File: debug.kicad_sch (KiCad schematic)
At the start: 4 parts, among them J3 FTSH-105-01-L-DV-007

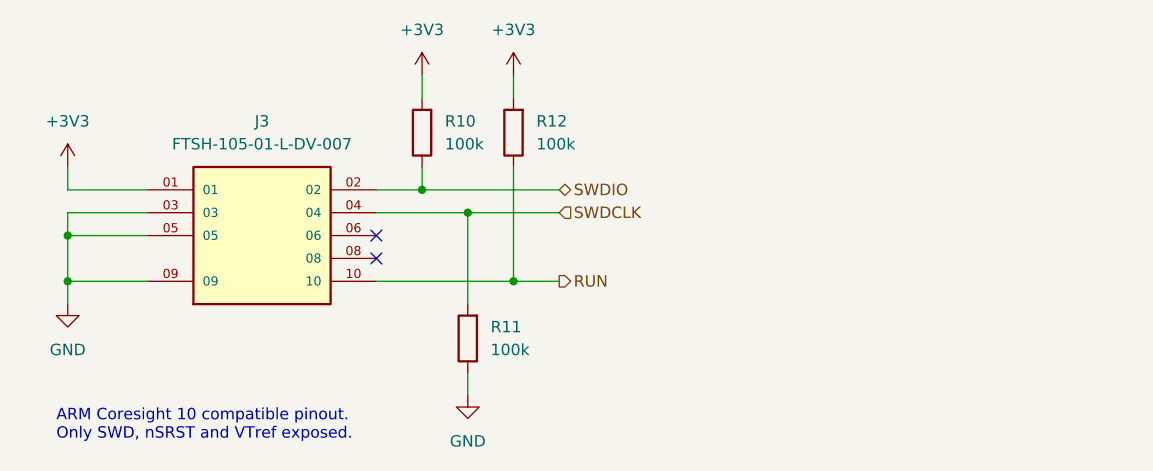
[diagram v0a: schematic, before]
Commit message: Block diagram
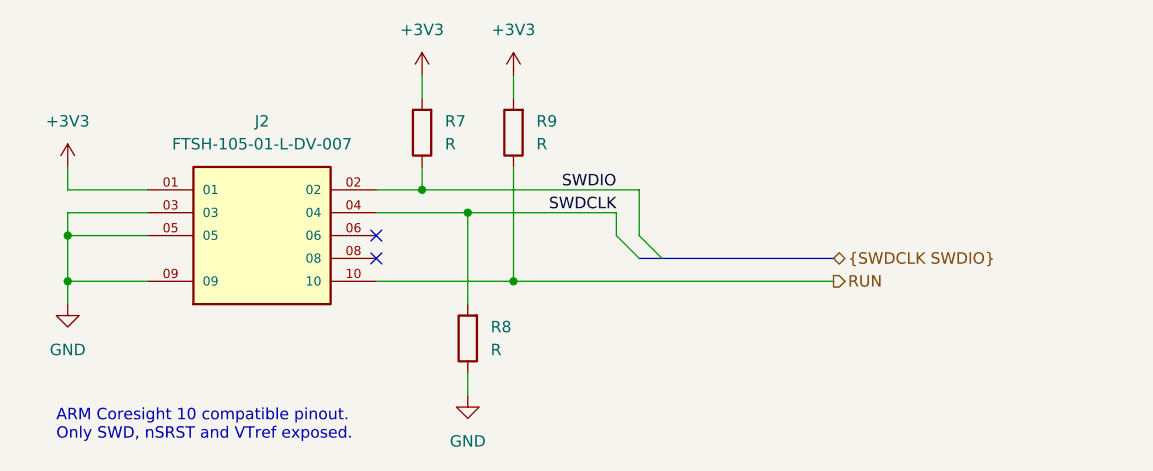
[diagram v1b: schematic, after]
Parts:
- R7: renamed from R10; value 100k -> R; footprint Resistor_SMD:R_1206_3216Metric -> Resistor_SMD:R_0402_1005Metric
- R8: renamed from R11; value 100k -> R; footprint Resistor_SMD:R_1206_3216Metric -> Resistor_SMD:R_0402_1005Metric
- R9: renamed from R12; value 100k -> R; footprint Resistor_SMD:R_1206_3216Metric -> Resistor_SMD:R_0402_1005Metric
- renumbered J3 to J2
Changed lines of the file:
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@@
 		(at 139.7 95.25)
 	)
+	(bus_entry
+		(at 166.37 95.25)
+		(size 2.54 2.54)
+		(stroke
+			(width 0)
+			(type default)
+		)
+	)
+	(bus_entry
+		(at 168.91 95.25)
+		(size 2.54 2.54)
+		(stroke
+			(width 0)
+			(type default)
+		)
+	)
 	(wire
 		(pts
@@
 	(wire
 		(pts
-			(xy 160.02 90.17) (xy 144.78 90.17)
+			(xy 144.78 90.17) (xy 168.91 90.17)
 		)
 		(stroke
@@
 	(wire
 		(pts
+			(xy 166.37 92.71) (xy 166.37 95.25)
+		)
+		(stroke
+			(width 0)
+			(type default)
+		)
+	)
+	(wire
+		(pts
 			(xy 139.7 100.33) (xy 154.94 100.33)
 		)
@@
 	(wire
 		(pts
-			(xy 149.86 92.71) (xy 160.02 92.71)
-		)
-		(stroke
-			(width 0)
-			(type default)
-		)
-	)
-	(wire
-		(pts
-			(xy 160.02 100.33) (xy 154.94 100.33)
+			(xy 149.86 92.71) (xy 166.37 92.71)
+		)
+		(stroke
+			(width 0)
+			(type default)
+		)
+	)
+	(wire
+		(pts
+			(xy 168.91 90.17) (xy 168.91 95.25)
+		)
+		(stroke
+			(width 0)
+			(type default)
+		)
+	)
+	(wire
+		(pts
+			(xy 190.5 100.33) (xy 154.94 100.33)
+		)
+		(stroke
+			(width 0)
+			(type default)
+		)
+	)
+	(bus
+		(pts
+			(xy 171.45 97.79) (xy 190.5 97.79)
 		)
 		(stroke
@@
 		(pts
 			(xy 149.86 110.49) (xy 149.86 113.03)
+		)
+		(stroke
+			(width 0)
+			(type default)
+		)
+	)
+	(bus
+		(pts
+			(xy 168.91 97.79) (xy 171.45 97.79)
 		)
 		(stroke
@@
 		)
 	)
-	(hierarchical_label "SWDCLK"
-		(shape input)
-		(at 160.02 92.71 0)
+	(label "SWDIO"
+		(at 166.37 90.17 180)
 		(fields_autoplaced yes)
 		(effects
@@
 				(size 1.27 1.27)
 			)
-			(justify left)
-		)
-	)
-	(hierarchical_label "SWDIO"
-		(shape bidirectional)
-		(at 160.02 90.17 0)
+			(justify right bottom)
+		)
+	)
+	(label "SWDCLK"
+		(at 166.37 92.71 180)
 		(fields_autoplaced yes)
 		(effects
@@
 				(size 1.27 1.27)
 			)
+			(justify right bottom)
+		)
+	)
+	(hierarchical_label "{SWDCLK SWDIO}"
+		(shape bidirectional)
+		(at 190.5 97.79 0)
+		(fields_autoplaced yes)
+		(effects
+			(font
+				(size 1.27 1.27)
+			)
 			(justify left)
 		)
@@
 	(hierarchical_label "RUN"
 		(shape output)
-		(at 160.02 100.33 0)
+		(at 190.5 100.33 0)
 		(fields_autoplaced yes)
 		(effects
@@
 		(dnp no)
 		(fields_autoplaced yes)
-		(property "Reference" "R11"
+		(property "Reference" "R8"
 			(at 152.4 105.41 0)
 			(effects
@@
 			)
 		)
-		(property "Value" "100k"
+		(property "Value" "R"
 			(at 152.4 107.95 0)
 			(effects
@@
 			)
 		)
-		(property "Footprint" "Resistor_SMD:R_1206_3216Metric"
+		(property "Footprint" "Resistor_SMD:R_0402_1005Metric"
 			(at 151.638 106.68 90)
 			(effects
@@
 			)
 		)
-		(property "Description" ""
+		(property "Description" "Resistor"
 			(at 149.86 106.68 0)
 			(effects
@@
 			(project "cubesat_rp2040"
 				(path "/5511013b-c214-40ba-8960-f470f52474f8/5047da3d-75a3-46e1-87b7-3e807ce5a802"
-					(reference "R11")
+					(reference "R8")
 					(unit 1)
 				)
@@
 		(dnp no)
 		(fields_autoplaced yes)
-		(property "Reference" "J3"
+		(property "Reference" "J2"
 			(at 127 82.55 0)
 			(effects
@@
 			(project "cubesat_rp2040"
 				(path "/5511013b-c214-40ba-8960-f470f52474f8/5047da3d-75a3-46e1-87b7-3e807ce5a802"
-					(reference "J3")
+					(reference "J2")
 					(unit 1)
 				)
@@
 		(dnp no)
 		(fields_autoplaced yes)
-		(property "Reference" "#PWR029"
+		(property "Reference" "#PWR019"
 			(at 154.94 81.28 0)
 			(effects
@@
 			)
 		)
-		(property "Description" ""
+		(property "Description" "Power symbol creates a global label with name \"+3V3\""
 			(at 154.94 77.47 0)
 			(effects
@@
 			(project "cubesat_rp2040"
 				(path "/5511013b-c214-40ba-8960-f470f52474f8/5047da3d-75a3-46e1-87b7-3e807ce5a802"
-					(reference "#PWR029")
+					(reference "#PWR019")
 					(unit 1)
 				)
@@
 		(dnp no)
 		(fields_autoplaced yes)
-		(property "Reference" "#PWR026"
+		(property "Reference" "#PWR016"
 			(at 105.41 109.22 0)
 			(effects
@@
 			)
 		)
-		(property "Description" ""
+		(property "Description" "Power symbol creates a global label with name \"GND\" , ground"
 			(at 105.41 102.87 0)
 			(effects
@@
 			(project "cubesat_rp2040"
 				(path "/5511013b-c214-40ba-8960-f470f52474f8/5047da3d-75a3-46e1-87b7-3e807ce5a802"
-					(reference "#PWR026")
+					(reference "#PWR016")
 					(unit 1)
 				)
@@
 		(dnp no)
 		(fields_autoplaced yes)
-		(property "Reference" "#PWR028"
+		(property "Reference" "#PWR018"
 			(at 149.86 119.38 0)
 			(effects
@@
 			)
 		)
-		(property "Description" ""
+		(property "Description" "Power symbol creates a global label with name \"GND\" , ground"
 			(at 149.86 113.03 0)
 			(effects
@@
 			(project "cubesat_rp2040"
 				(path "/5511013b-c214-40ba-8960-f470f52474f8/5047da3d-75a3-46e1-87b7-3e807ce5a802"
-					(reference "#PWR028")
+					(reference "#PWR018")
 					(unit 1)
 				)
@@
 		(dnp no)
 		(fields_autoplaced yes)
-		(property "Reference" "R10"
+		(property "Reference" "R7"
 			(at 147.32 82.55 0)
 			(effects
@@
 			)
 		)
-		(property "Value" "100k"
+		(property "Value" "R"
 			(at 147.32 85.09 0)
 			(effects
@@
 			)
 		)
-		(property "Footprint" "Resistor_SMD:R_1206_3216Metric"
+		(property "Footprint" "Resistor_SMD:R_0402_1005Metric"
 			(at 146.558 83.82 90)
 			(effects
@@
 			)
 		)
-		(property "Description" ""
+		(property "Description" "Resistor"
 			(at 144.78 83.82 0)
 			(effects
@@
 			(project "cubesat_rp2040"
 				(path "/5511013b-c214-40ba-8960-f470f52474f8/5047da3d-75a3-46e1-87b7-3e807ce5a802"
-					(reference "R10")
+					(reference "R7")
 					(unit 1)
 				)
@@
 		(dnp no)
 		(fields_autoplaced yes)
-		(property "Reference" "#PWR025"
+		(property "Reference" "#PWR015"
 			(at 105.41 91.44 0)
 			(effects
@@
 			)
 		)
-		(property "Description" ""
+		(property "Description" "Power symbol creates a global label with name \"+3V3\""
 			(at 105.41 87.63 0)
 			(effects
@@
 			(project "cubesat_rp2040"
 				(path "/5511013b-c214-40ba-8960-f470f52474f8/5047da3d-75a3-46e1-87b7-3e807ce5a802"
-					(reference "#PWR025")
+					(reference "#PWR015")
 					(unit 1)
 				)
@@
 		(dnp no)
 		(fields_autoplaced yes)
-		(property "Reference" "#PWR027"
+		(property "Reference" "#PWR017"
 			(at 144.78 81.28 0)
 			(effects
@@
 			)
 		)
-		(property "Description" ""
+		(property "Description" "Power symbol creates a global label with name \"+3V3\""
 			(at 144.78 77.47 0)
 			(effects
@@
 			(project "cubesat_rp2040"
 				(path "/5511013b-c214-40ba-8960-f470f52474f8/5047da3d-75a3-46e1-87b7-3e807ce5a802"
-					(reference "#PWR027")
+					(reference "#PWR017")
 					(unit 1)
 				)
@@
 		(dnp no)
 		(fields_autoplaced yes)
-		(property "Reference" "R12"
+		(property "Reference" "R9"
 			(at 157.48 82.55 0)
 			(effects
@@
 			)
 		)
-		(property "Value" "100k"
+		(property "Value" "R"
 			(at 157.48 85.09 0)
 			(effects
@@
 			)
 		)
-		(property "Footprint" "Resistor_SMD:R_1206_3216Metric"
+		(property "Footprint" "Resistor_SMD:R_0402_1005Metric"
 			(at 156.718 83.82 90)
 			(effects
@@
 			)
 		)
-		(property "Description" ""
+		(property "Description" "Resistor"
 			(at 154.94 83.82 0)
 			(effects
@@
 			(project "cubesat_rp2040"
 				(path "/5511013b-c214-40ba-8960-f470f52474f8/5047da3d-75a3-46e1-87b7-3e807ce5a802"
-					(reference "R12")
+					(reference "R9")
 					(unit 1)
 				)

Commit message: Big update, bad commit messsage :)
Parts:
- J401: renamed from J2; symbol cubesat_rp2040:FTSH-105-01-L-DV-007 -> cubesat_rp2040:CoreSight_10_Conn
- R401: renamed from R7; footprint Resistor_SMD:R_0402_1005Metric -> cubesat_rp2040:R_0402_1005Metric
- R402: renamed from R8; footprint Resistor_SMD:R_0402_1005Metric -> cubesat_rp2040:R_0402_1005Metric
- R403: renamed from R9; footprint Resistor_SMD:R_0402_1005Metric -> cubesat_rp2040:R_0402_1005Metric
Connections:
- net RUN renamed ~{RESET}
- net SWDCLK renamed SWCLK
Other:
- company: (none) -> Magnus Oksbøl Therkelsen
- title: (none) -> CubeSat RP2040 Board
- moved on the sheet: J401, R401, R402, R403
